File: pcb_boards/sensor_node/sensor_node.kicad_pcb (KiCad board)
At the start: 2 copper layers, 93 x 93 mm, 58 parts, among them IC1 PCF2129T, J1 Screw_Terminal_01x15, J2 Conn_02x03_Odd_Even, J3 USB_B_Micro, J4 Screw_Terminal_01x12, U1 SiP32431, U2 ESP32-WROOM-32, U3 RF-LORA-868-SO, U4 FT232RL, U7 RP604x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

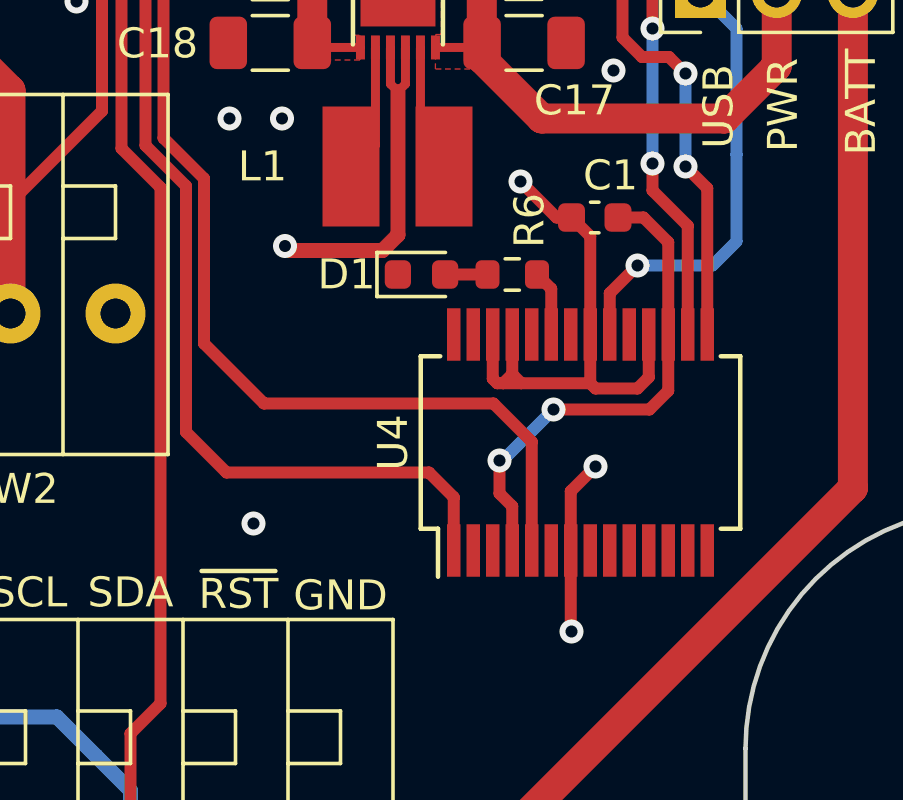
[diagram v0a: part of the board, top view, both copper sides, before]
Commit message: Switch USB programmer UART lines; fix LED
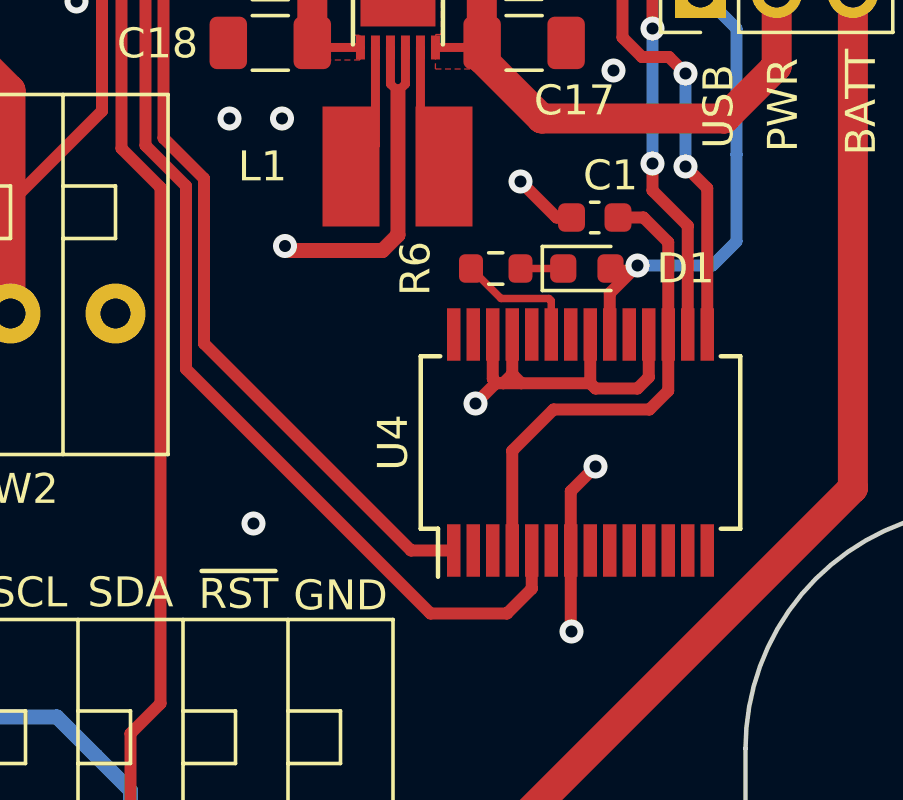
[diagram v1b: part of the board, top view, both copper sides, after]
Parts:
- R6: value 60R -> 750R
- moved D1 5.52 mm to (117.7, 105.5)
- moved R6 0.59 mm to (114.7, 105.5), turned to 0 degrees
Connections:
- D1 pad 1: GND -> Net-(D1-K)
- D1 pad 2: Net-(D1-Pad2) -> VBUS
- R6 pad 2: Net-(D1-Pad2) -> Net-(D1-K)
- U4 pad 1: /TX -> /RX
- U4 pad 5: /RX -> /TX
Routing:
- net /RX: track 80.1 -> 75.4 mm
- net GND: track 77.2 -> 74.0 mm, vias 77 -> 78
- net /TX: track 74.1 -> 76.9 mm
- net Net-(U4-CBUS0): track 2.20 -> 4.25 mm
- net Net-(D1-K): track 0.00 -> 1.42 mm
- net Net-(D1-Pad2): track 1.41 -> 0.00 mm
- net VBUS: track 21.9 -> 22.8 mm
- net Net-(U4-3V3OUT): track 16.7 -> 16.3 mm, vias 2 -> 0

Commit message: Make USB connector vertical; fix tiny errors
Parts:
- J3: footprint Connector_USB:USB_Micro-B_Molex-105017-0001 -> Connector_USB:USB_Micro-B_Molex-105133-0001
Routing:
- net GND: track 74.0 -> 85.0 mm
- net Net-(D3-A): track 5.52 -> 6.16 mm
- net /D-: track 35.1 -> 35.7 mm
- net /D+: track 37.0 -> 37.6 mm
